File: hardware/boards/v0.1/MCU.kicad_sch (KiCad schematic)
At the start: 38 parts, among them SW24 NRST, SW25 BOOT0, U1 BMDU, U18 STM32H743ZIT6, Y1 7E032768H01, Y4 X322525MOB4SI

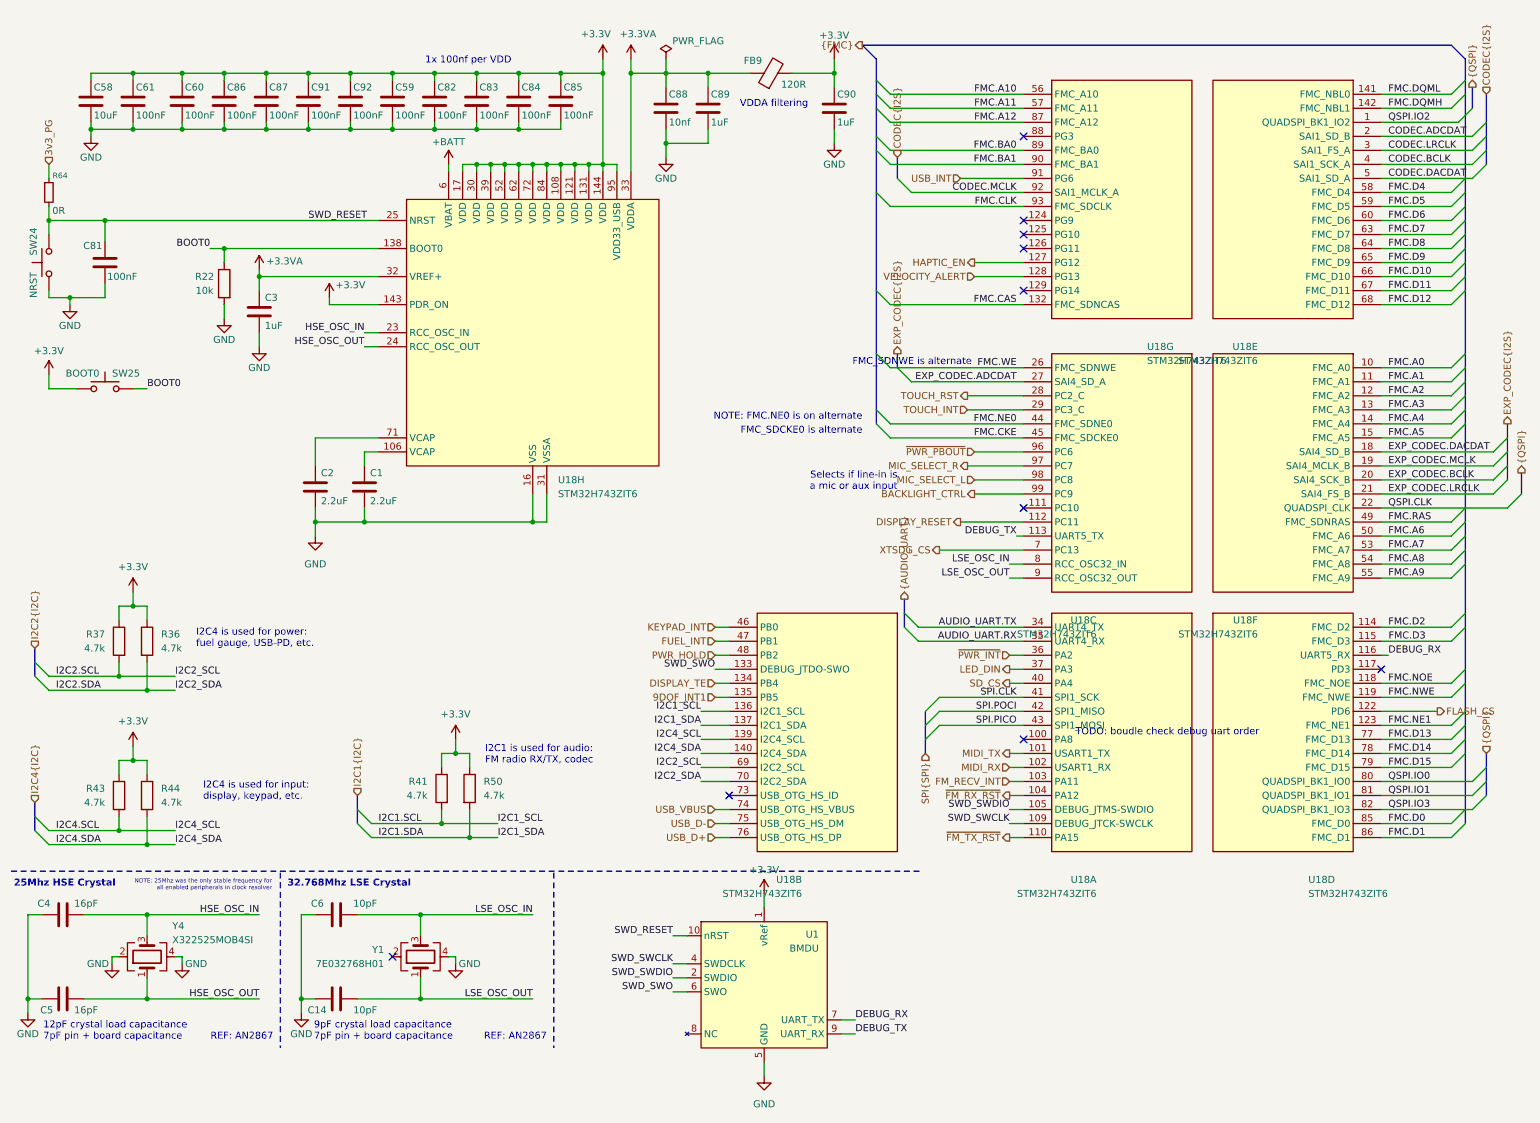
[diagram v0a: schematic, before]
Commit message: feat: add power LEDs and adjust layout
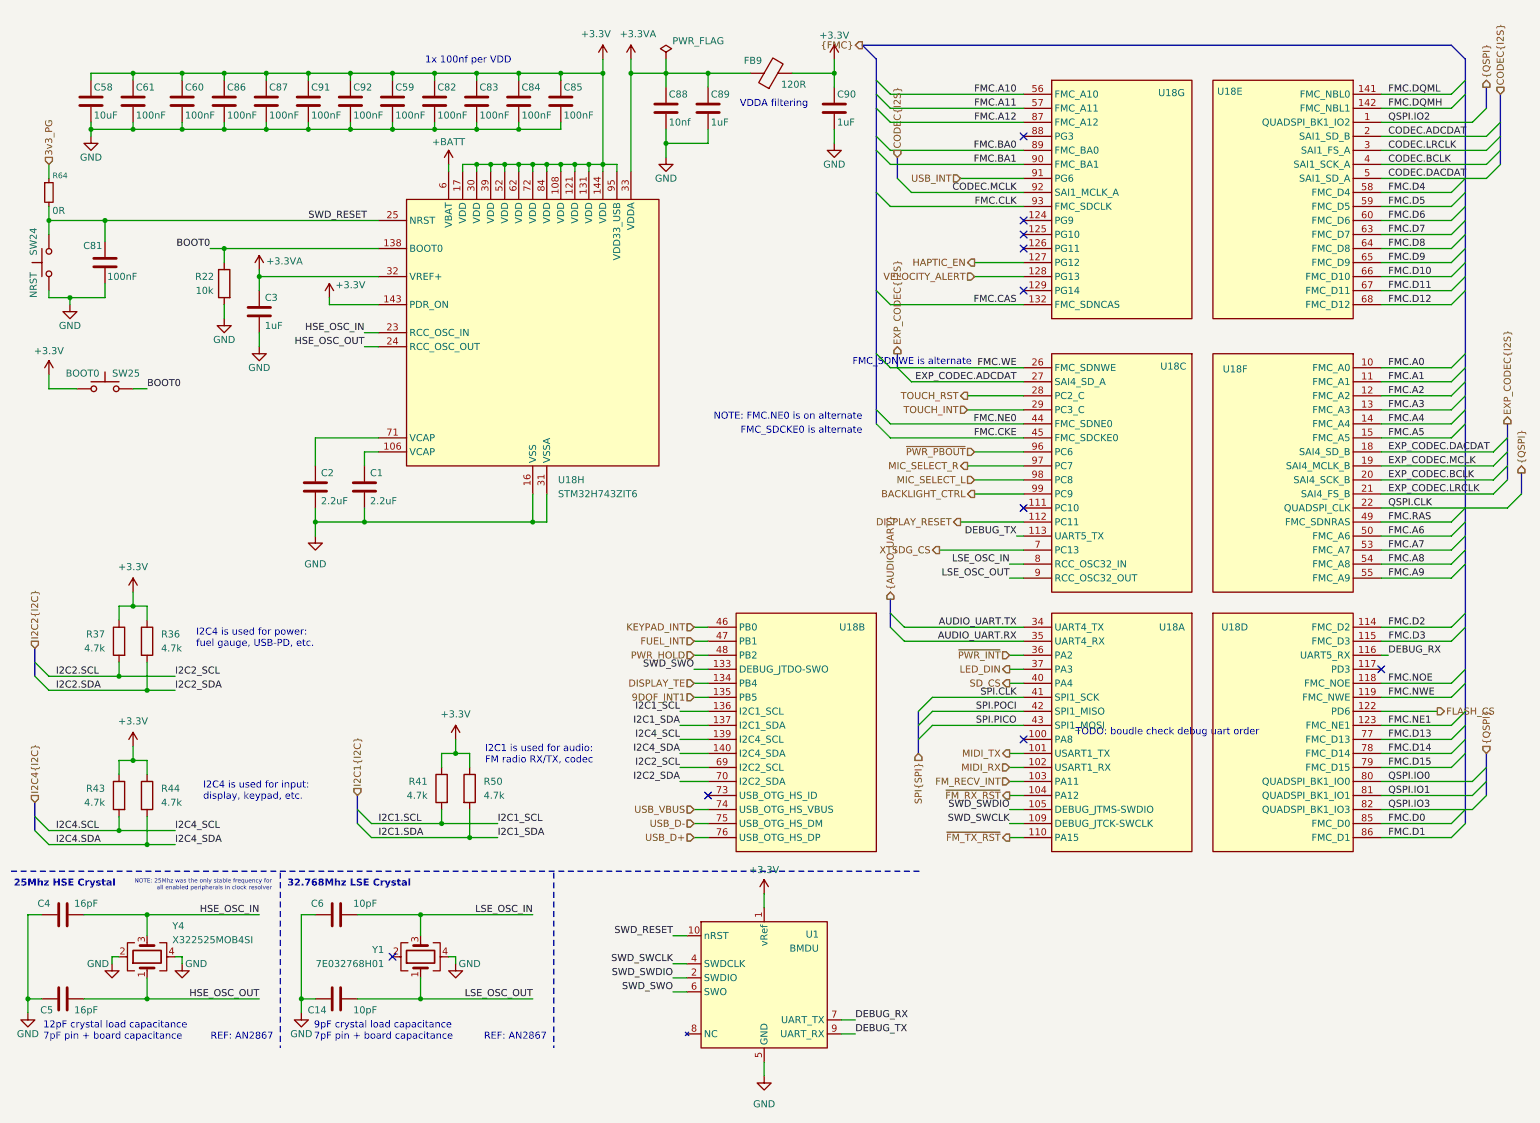
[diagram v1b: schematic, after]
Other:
- note removed: "Selects if line-in is a mic or aux input"
- moved on the sheet: U18B

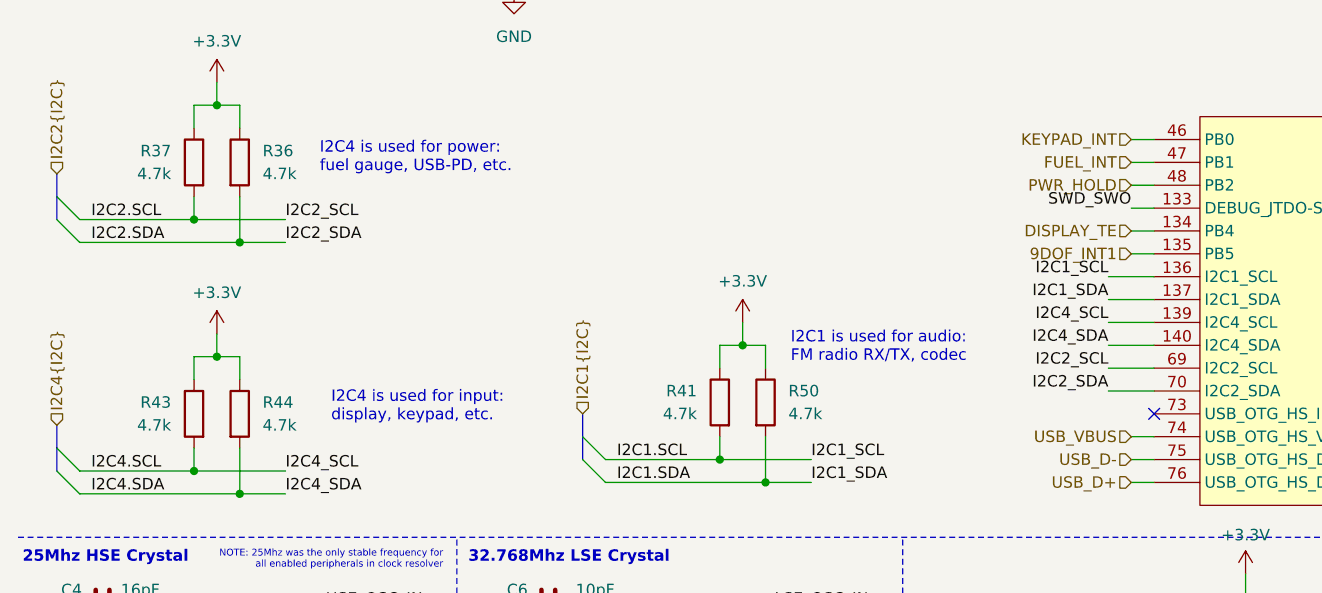
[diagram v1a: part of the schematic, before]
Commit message: feat: change charger, fuel gauge, and battery connector, re-route power system
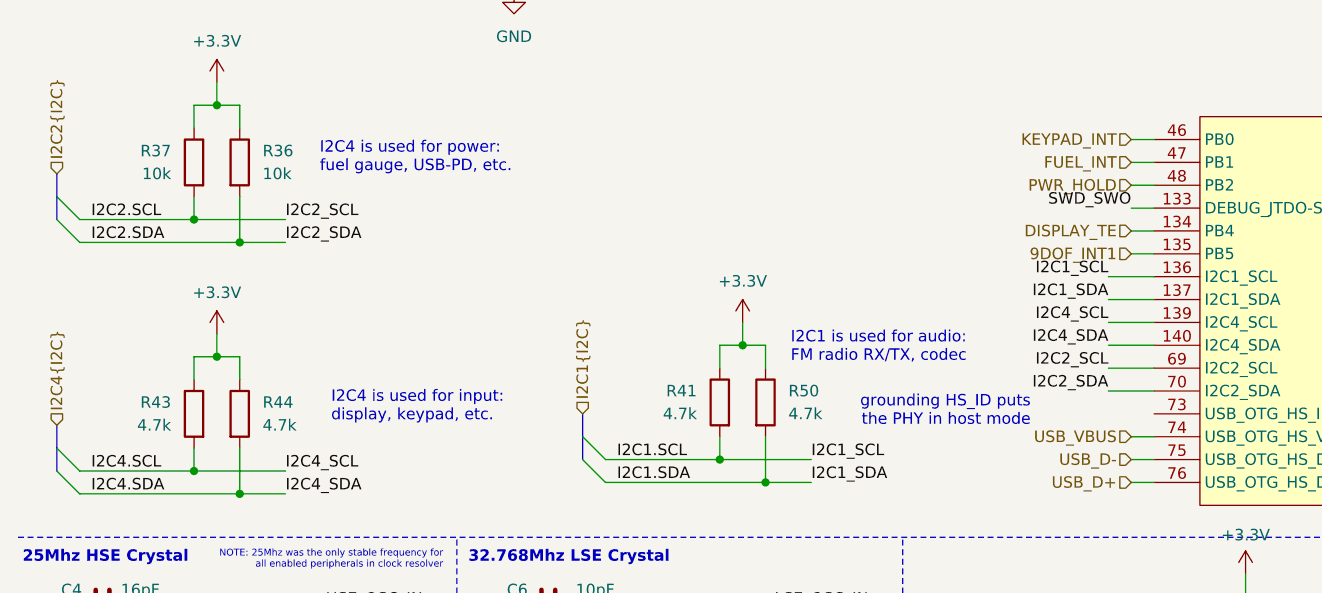
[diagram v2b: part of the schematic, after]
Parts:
- C3, C89, C90: JLC C14445 -> C52923
- R22: JLC C25531 -> C25744
- R36, R37: value 4.7k -> 10k; JLC C25900 -> C25744
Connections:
- no-connect marks 10 -> 9
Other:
- note added: "grounding HS_ID puts the PHY in host mode"
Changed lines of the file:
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@@
 		)
 	)
+	(text "grounding HS_ID puts\nthe PHY in host mode"
+		(exclude_from_sim no)
+		(at 124.714 152.146 0)
+		(effects
+			(font
+				(size 1.27 1.27)
+				(color 132 132 132 1)
+			)
+			(justify right)
+		)
+	)
 	(text "NOTE: FMC.NE0 is on alternate"
 		(exclude_from_sim no)
@@
 	)
 	(no_connect
-		(at 138.43 152.4)
-	)
-	(no_connect
 		(at 195.58 142.24)
 	)
@@
 			)
 		)
-		(property "JLC" "C14445"
+		(property "JLC" "C52923"
 			(at 138.43 27.94 0)
 			(effects
@@
 			)
 		)
-		(property "JLC" "C14445"
+		(property "JLC" "C52923"
 			(at 161.29 27.94 0)
 			(effects
@@
 			)
 		)
-		(property "JLC" "C25531"
+		(property "JLC" "C25744"
 			(at 50.8 59.69 0)
 			(effects
@@
 			)
 		)
-		(property "JLC" "C14445"
+		(property "JLC" "C52923"
 			(at 57.15 64.77 0)
 			(effects
@@
 			)
 		)
-		(property "Value" "4.7k"
+		(property "Value" "10k"
 			(at 39.37 125.7299 0)
 			(effects
@@
 			)
 		)
-		(property "JLC" "C25900"
+		(property "JLC" "C25744"
 			(at 36.83 124.46 0)
 			(effects
@@
 			)
 		)
-		(property "Value" "4.7k"
+		(property "Value" "10k"
 			(at 29.21 125.7299 0)
 			(effects
@@
 			)
 		)
-		(property "JLC" "C25900"
+		(property "JLC" "C25744"
 			(at 31.75 124.46 0)
 			(effects

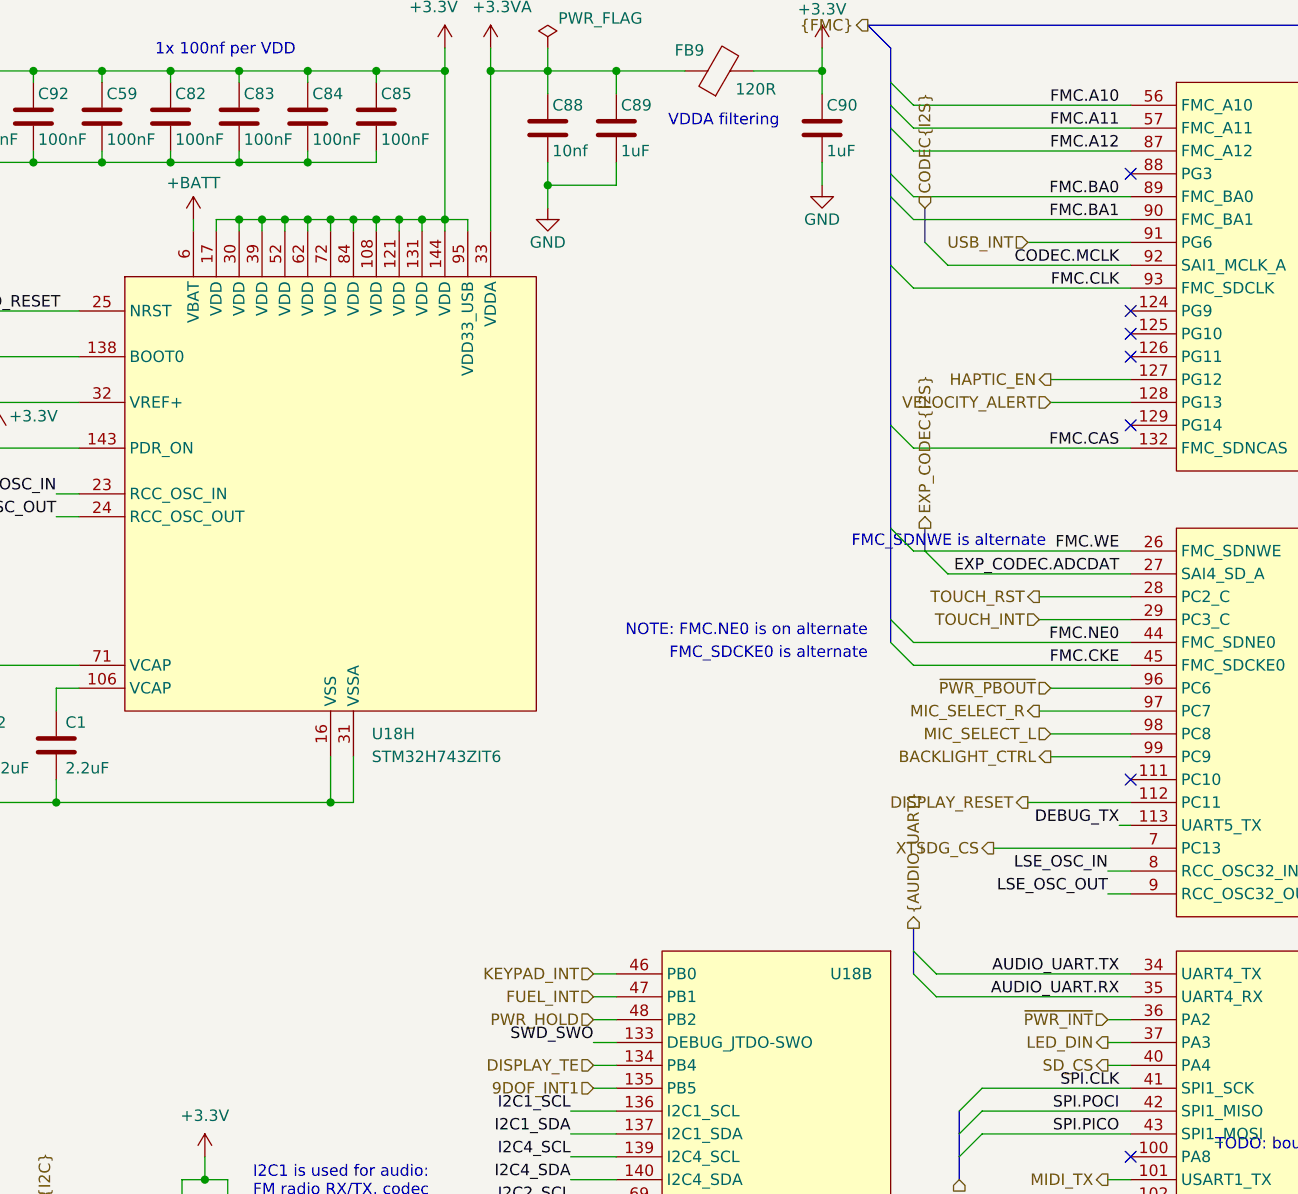
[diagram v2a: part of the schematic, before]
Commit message: feat: finish routing new power circuit
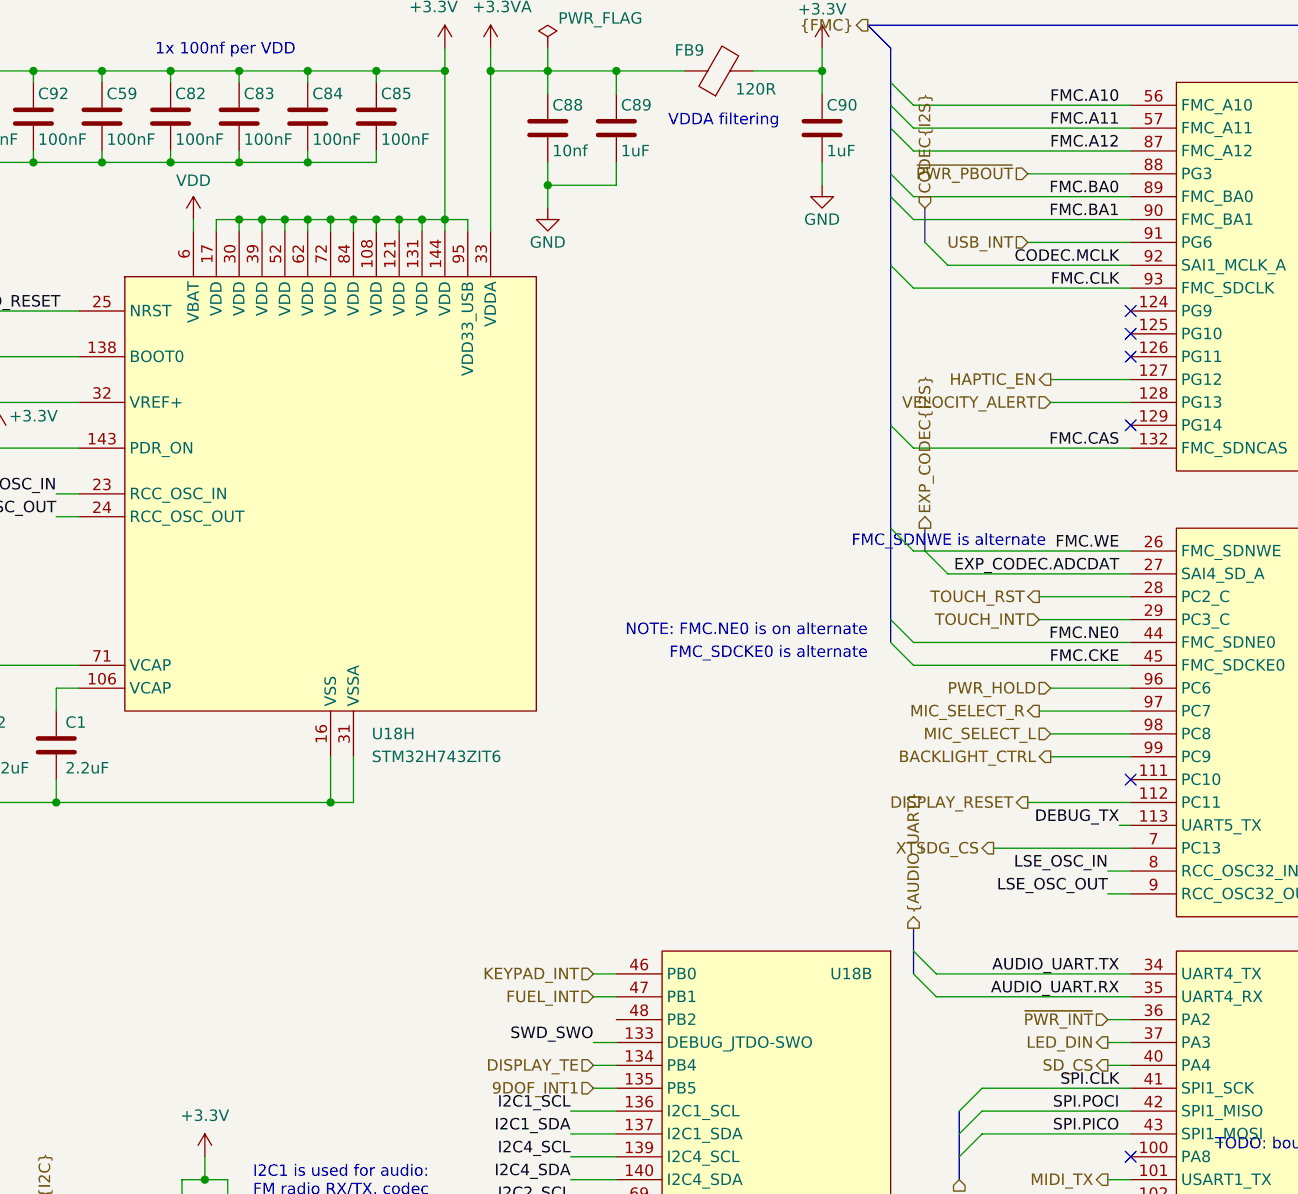
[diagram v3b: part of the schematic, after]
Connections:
- net PWR_HOLD: now also U18.96 (PC6); no longer U18.48 (PB2)
- net ~{PWR_PBOUT}: now also U18.88 (PG3); no longer U18.96 (PC6)
- net +BATT renamed VDD
- no-connect marks 9 -> 8
